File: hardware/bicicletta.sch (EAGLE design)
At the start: 27 parts, among them IC1 LM5017, IC2 LM1117-3.3

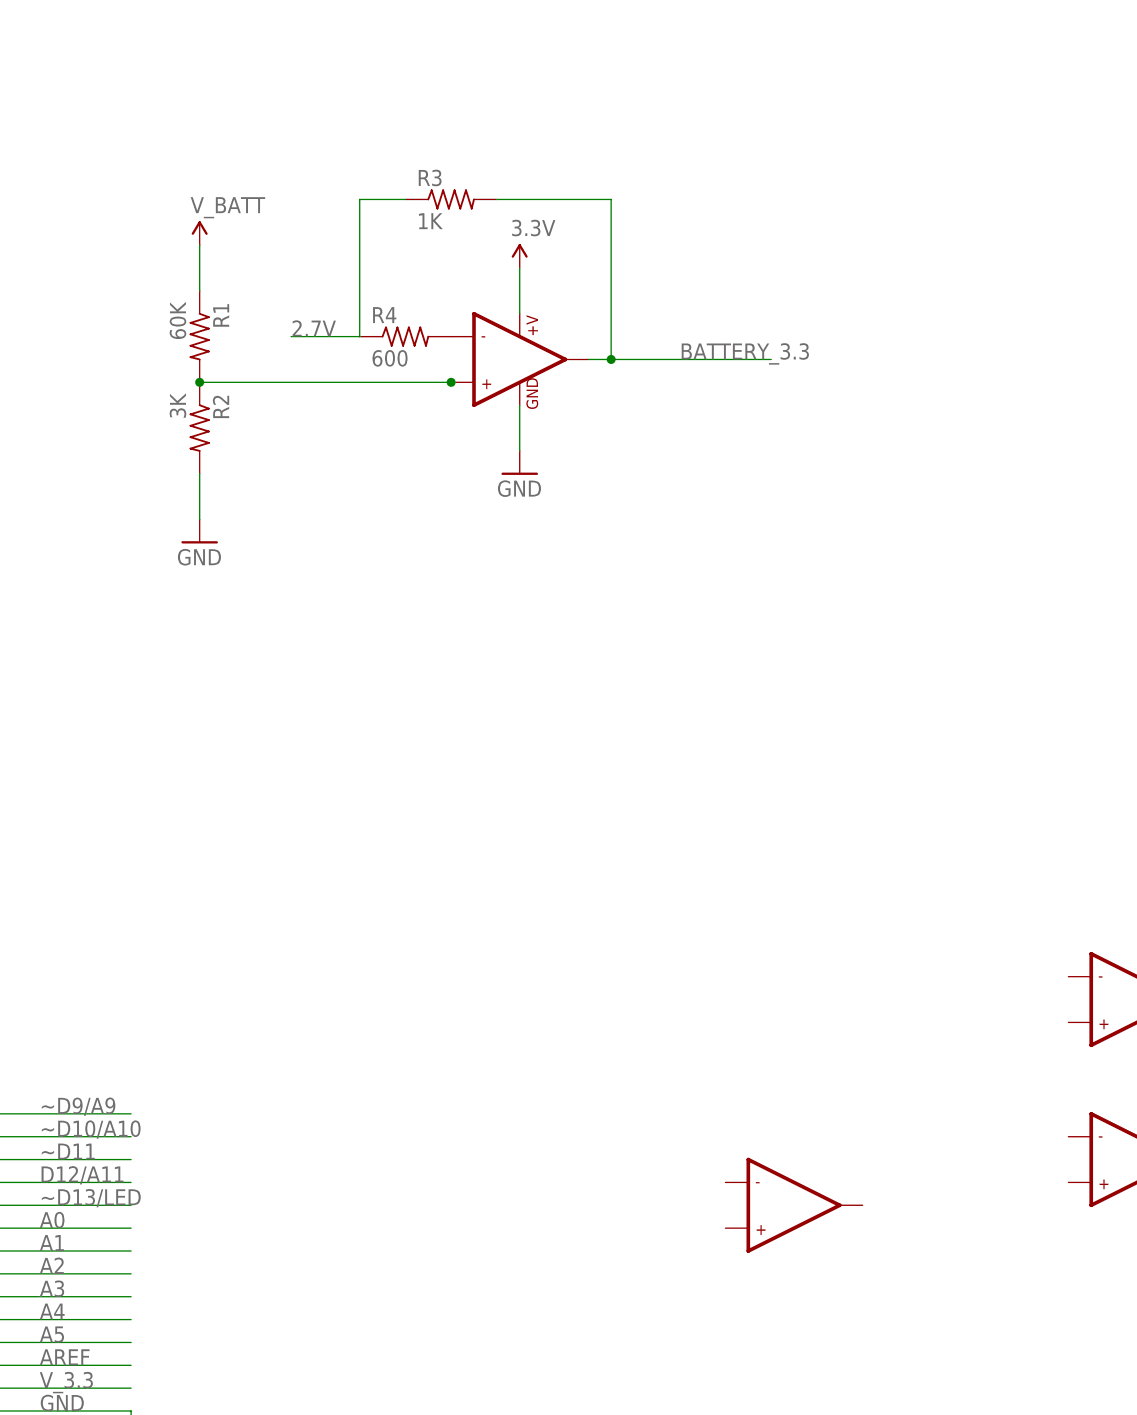
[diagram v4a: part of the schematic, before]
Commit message: Fixed battery voltage shifter, added level shifter for throttle (5V hall effect sensor)
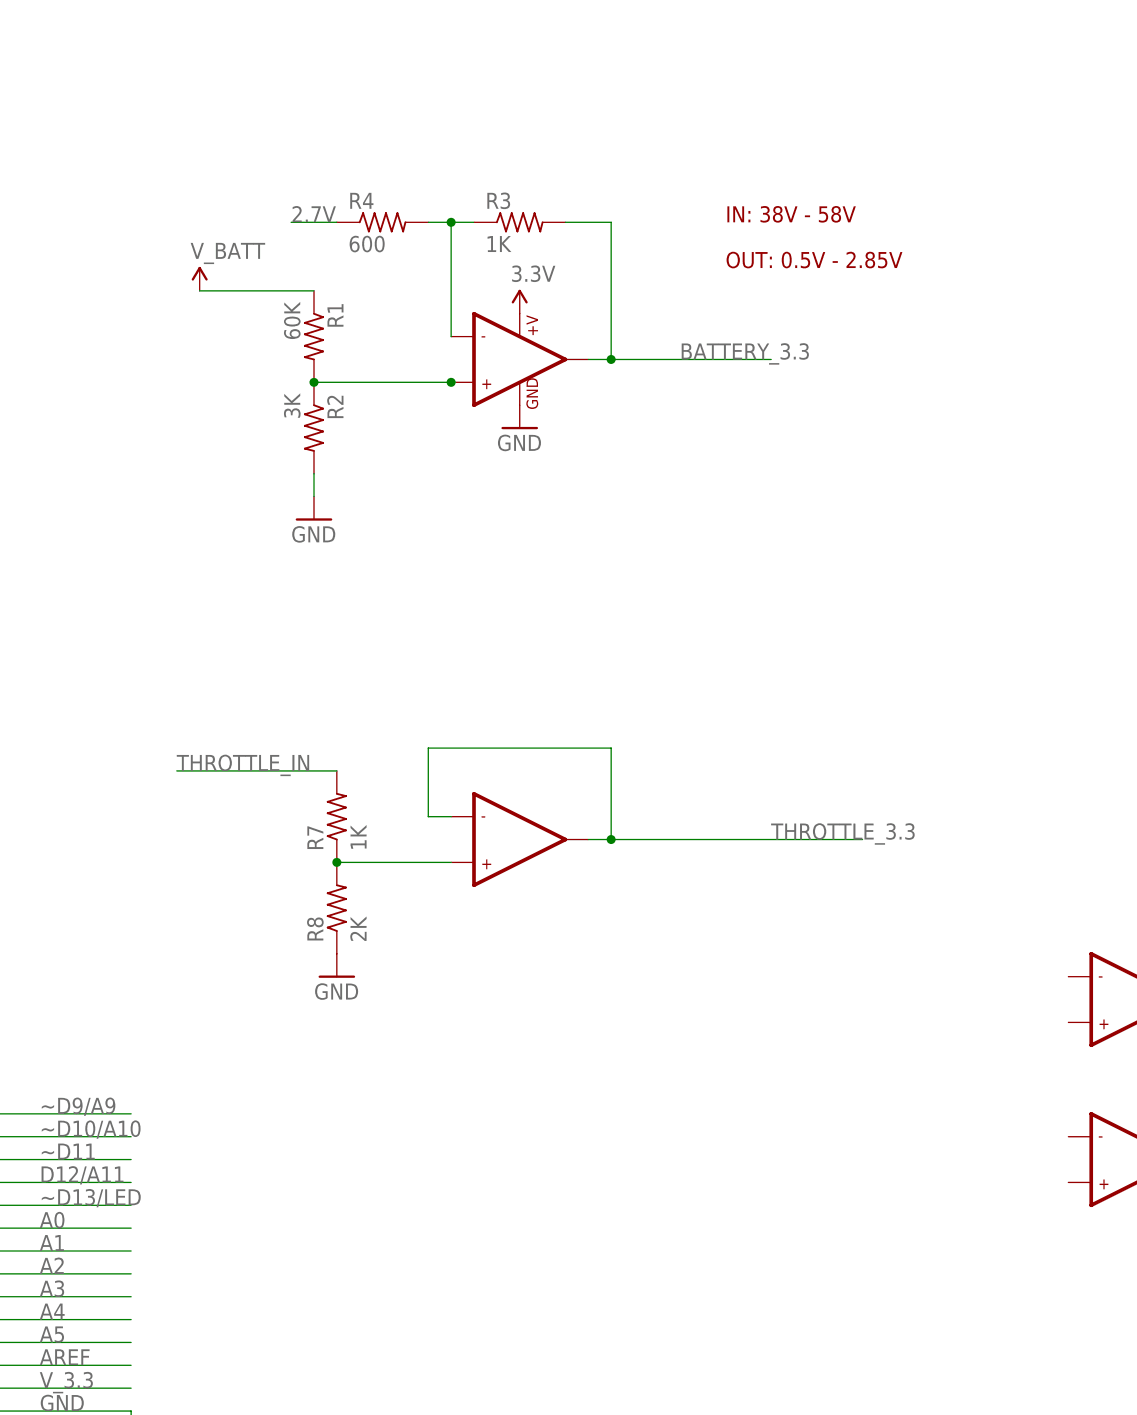
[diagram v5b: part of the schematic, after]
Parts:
- added R7: 1K, rcl:R-US_M0805
- added R8: 2K, rcl:R-US_M0805
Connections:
- new net N$11: R7.1, R8.2, U$1G$2.+IN2
- new net THROTTLE_3.3: U$1G$2.-IN2, U$1G$2.OUT2
- new net THROTTLE_IN: R7.2
- net 2.7V: no longer R3.1
- net GND: now also R8.1
- net N$10: now also R3.1
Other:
- note added: "IN: 38V - 58V"
- note added: "OUT: 0.5V - 2.85V"
- moved on the sheet: R1, R2, R3, R4
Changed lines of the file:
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@@
 <part name="GND7" library="SparkFun-Aesthetics" deviceset="GND" device=""/>
 <part name="U$4" library="SparkFun-Aesthetics" deviceset="V_BATT" device=""/>
+<part name="R7" library="rcl" deviceset="R-US_" device="M0805" value="1K"/>
+<part name="R8" library="rcl" deviceset="R-US_" device="M0805" value="2K"/>
+<part name="GND8" library="SparkFun-Aesthetics" deviceset="GND" device=""/>
 </parts>
 <sheets>
 <sheet>
 <plain>
+<text x="162.56" y="170.18" size="1.778" layer="94">IN: 38V - 58V</text>
+<text x="162.56" y="165.1" size="1.778" layer="94">OUT: 0.5V - 2.85V</text>
 </plain>
 <instances>
@@
 <instance part="JP2" gate="G$1" x="71.12" y="55.88"/>
 <instance part="U$1" gate="G$1" x="139.7" y="154.94"/>
-<instance part="U$1" gate="G$2" x="170.18" y="60.96"/>
+<instance part="U$1" gate="G$2" x="139.7" y="101.6"/>
 <instance part="U$2" gate="G$1" x="208.28" y="83.82"/>
 <instance part="U$2" gate="G$2" x="208.28" y="66.04"/>
@@
 <instance part="C1" gate="G$1" x="172.72" y="236.22"/>
 <instance part="C2" gate="G$1" x="208.28" y="236.22"/>
-<instance part="R1" gate="G$1" x="104.14" y="157.48" rot="R270"/>
-<instance part="R2" gate="G$1" x="104.14" y="147.32" rot="R270"/>
-<instance part="GND5" gate="1" x="104.14" y="134.62"/>
-<instance part="R3" gate="G$1" x="132.08" y="172.72"/>
-<instance part="R4" gate="G$1" x="127" y="157.48"/>
+<instance part="R1" gate="G$1" x="116.84" y="157.48" rot="R270"/>
+<instance part="R2" gate="G$1" x="116.84" y="147.32" rot="R270"/>
+<instance part="GND5" gate="1" x="116.84" y="137.16"/>
+<instance part="R3" gate="G$1" x="139.7" y="170.18"/>
+<instance part="R4" gate="G$1" x="124.46" y="170.18"/>
 <instance part="R5" gate="G$1" x="55.88" y="157.48" rot="R90"/>
 <instance part="R6" gate="G$1" x="55.88" y="147.32" rot="R90"/>
-<instance part="GND6" gate="1" x="139.7" y="142.24"/>
-<instance part="P+2" gate="G$1" x="139.7" y="165.1"/>
+<instance part="GND6" gate="1" x="139.7" y="147.32"/>
+<instance part="P+2" gate="G$1" x="139.7" y="160.02"/>
 <instance part="P+3" gate="G$1" x="55.88" y="165.1"/>
 <instance part="GND7" gate="1" x="55.88" y="137.16"/>
-<instance part="U$4" gate="G$1" x="104.14" y="167.64"/>
+<instance part="U$4" gate="G$1" x="104.14" y="162.56"/>
+<instance part="R7" gate="G$1" x="119.38" y="104.14" rot="R90"/>
+<instance part="R8" gate="G$1" x="119.38" y="93.98" rot="R90"/>
+<instance part="GND8" gate="1" x="119.38" y="86.36"/>
 </instances>
 <busses>
@@
 <pinref part="R2" gate="G$1" pin="2"/>
 <pinref part="GND5" gate="1" pin="GND"/>
-<wire x1="104.14" y1="137.16" x2="104.14" y2="142.24" width="0.1524" layer="91"/>
+<wire x1="116.84" y1="139.7" x2="116.84" y2="142.24" width="0.1524" layer="91"/>
 </segment>
 <segment>
 <pinref part="U$1" gate="G$1" pin="GND"/>
 <pinref part="GND6" gate="1" pin="GND"/>
-<wire x1="139.7" y1="144.78" x2="139.7" y2="149.86" width="0.1524" layer="91"/>
 </segment>
 <segment>
@@
 <wire x1="55.88" y1="139.7" x2="55.88" y2="142.24" width="0.1524" layer="91"/>
 <pinref part="GND7" gate="1" pin="GND"/>
+</segment>
+<segment>
+<pinref part="R8" gate="G$1" pin="1"/>
+<pinref part="GND8" gate="1" pin="GND"/>
 </segment>
 </net>
@@
 <segment>
 <pinref part="R1" gate="G$1" pin="1"/>
-<wire x1="104.14" y1="167.64" x2="104.14" y2="162.56" width="0.1524" layer="91"/>
+<wire x1="104.14" y1="162.56" x2="116.84" y2="162.56" width="0.1524" layer="91"/>
 <pinref part="U$4" gate="G$1" pin="1.8V"/>
 </segment>
@@
 <pinref part="U$1" gate="G$1" pin="+V"/>
 <pinref part="P+2" gate="G$1" pin="3.3V"/>
-<wire x1="139.7" y1="165.1" x2="139.7" y2="160.02" width="0.1524" layer="91"/>
 </segment>
 <segment>
@@
 <junction x="132.08" y="152.4"/>
 <pinref part="U$1" gate="G$1" pin="+IN1"/>
-<wire x1="132.08" y1="152.4" x2="104.14" y2="152.4" width="0.1524" layer="91"/>
-<junction x="104.14" y="152.4"/>
+<wire x1="132.08" y1="152.4" x2="116.84" y2="152.4" width="0.1524" layer="91"/>
+<junction x="116.84" y="152.4"/>
 </segment>
 </net>
@@
 <pinref part="R3" gate="G$1" pin="2"/>
 <wire x1="149.86" y1="154.94" x2="167.64" y2="154.94" width="0.1524" layer="91"/>
-<wire x1="137.16" y1="172.72" x2="149.86" y2="172.72" width="0.1524" layer="91"/>
-<wire x1="149.86" y1="172.72" x2="149.86" y2="154.94" width="0.1524" layer="91"/>
+<wire x1="144.78" y1="170.18" x2="149.86" y2="170.18" width="0.1524" layer="91"/>
+<wire x1="149.86" y1="170.18" x2="149.86" y2="154.94" width="0.1524" layer="91"/>
 <junction x="149.86" y="154.94"/>
 </segment>
@@
 <segment>
 <pinref part="R4" gate="G$1" pin="2"/>
+<pinref part="R3" gate="G$1" pin="1"/>
+<wire x1="129.54" y1="170.18" x2="132.08" y2="170.18" width="0.1524" layer="91"/>
 <pinref part="U$1" gate="G$1" pin="-IN1"/>
+<wire x1="132.08" y1="170.18" x2="134.62" y2="170.18" width="0.1524" layer="91"/>
+<wire x1="132.08" y1="157.48" x2="132.08" y2="170.18" width="0.1524" layer="91"/>
+<junction x="132.08" y="170.18"/>
 </segment>
 </net>
 <net name="2.7V" class="0">
-<segment>
-<pinref part="R3" gate="G$1" pin="1"/>
-<pinref part="R4" gate="G$1" pin="1"/>
-<wire x1="127" y1="172.72" x2="121.92" y2="172.72" width="0.1524" layer="91"/>
-<wire x1="121.92" y1="172.72" x2="121.92" y2="157.48" width="0.1524" layer="91"/>
-<label x="114.3" y="157.48" size="1.778" layer="95"/>
-<wire x1="121.92" y1="157.48" x2="114.3" y2="157.48" width="0.1524" layer="91"/>
-</segment>
 <segment>
 <pinref part="R6" gate="G$1" pin="2"/>
@@
 <label x="63.5" y="152.4" size="1.778" layer="95"/>
 </segment>
-</net>
+<segment>
+<pinref part="R4" gate="G$1" pin="1"/>
+<wire x1="119.38" y1="170.18" x2="114.3" y2="170.18" width="0.1524" layer="91"/>
+<label x="114.3" y="170.18" size="1.778" layer="95"/>
+</segment>
+</net>
+<net name="THROTTLE_IN" class="0">
+<segment>
+<label x="101.6" y="109.22" size="1.778" layer="95"/>
+<wire x1="119.38" y1="109.22" x2="101.6" y2="109.22" width="0.1524" layer="91"/>
+<pinref part="R7" gate="G$1" pin="2"/>
+</segment>
+</net>
+<net name="THROTTLE_3.3" class="0">
+<segment>
+<pinref part="U$1" gate="G$2" pin="OUT2"/>
+<label x="167.64" y="101.6" size="1.778" layer="95"/>
+<wire x1="147.32" y1="101.6" x2="149.86" y2="101.6" width="0.1524" layer="91"/>
+<pinref part="U$1" gate="G$2" pin="-IN2"/>
+<wire x1="149.86" y1="101.6" x2="177.8" y2="101.6" width="0.1524" layer="91"/>
+<wire x1="132.08" y1="104.14" x2="129.54" y2="104.14" width="0.1524" layer="91"/>
+<wire x1="129.54" y1="104.14" x2="129.54" y2="111.76" width="0.1524" layer="91"/>
+<wire x1="129.54" y1="111.76" x2="149.86" y2="111.76" width="0.1524" layer="91"/>
+<wire x1="149.86" y1="111.76" x2="149.86" y2="101.6" width="0.1524" layer="91"/>
+<junction x="149.86" y="101.6"/>
+</segment>
+</net>
+<net name="N$11" class="0">
+<segment>
+<pinref part="R7" gate="G$1" pin="1"/>
+<pinref part="R8" gate="G$1" pin="2"/>
+<pinref part="U$1" gate="G$2" pin="+IN2"/>
+<wire x1="132.08" y1="99.06" x2="119.38" y2="99.06" width="0.1524" layer="91"/>
+<junction x="119.38" y="99.06"/>
+</segment>
+</net>

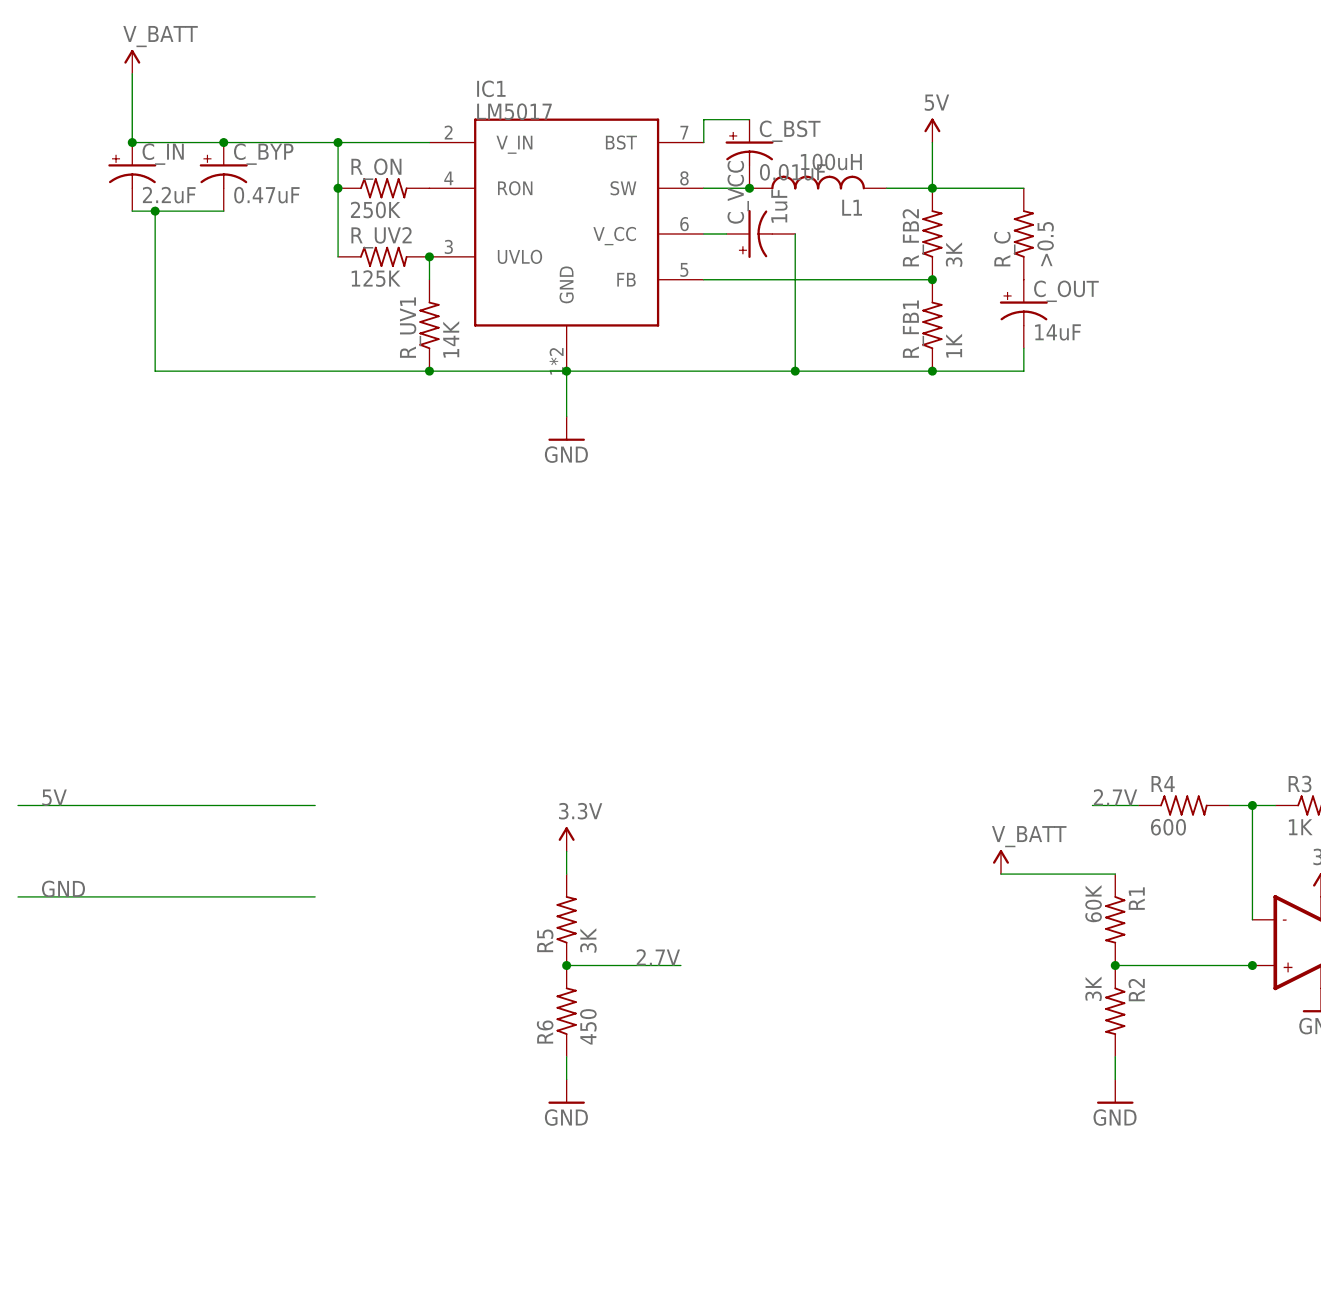
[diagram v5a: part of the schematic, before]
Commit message: Refactored the ripple feedback circuit on the switching regulator
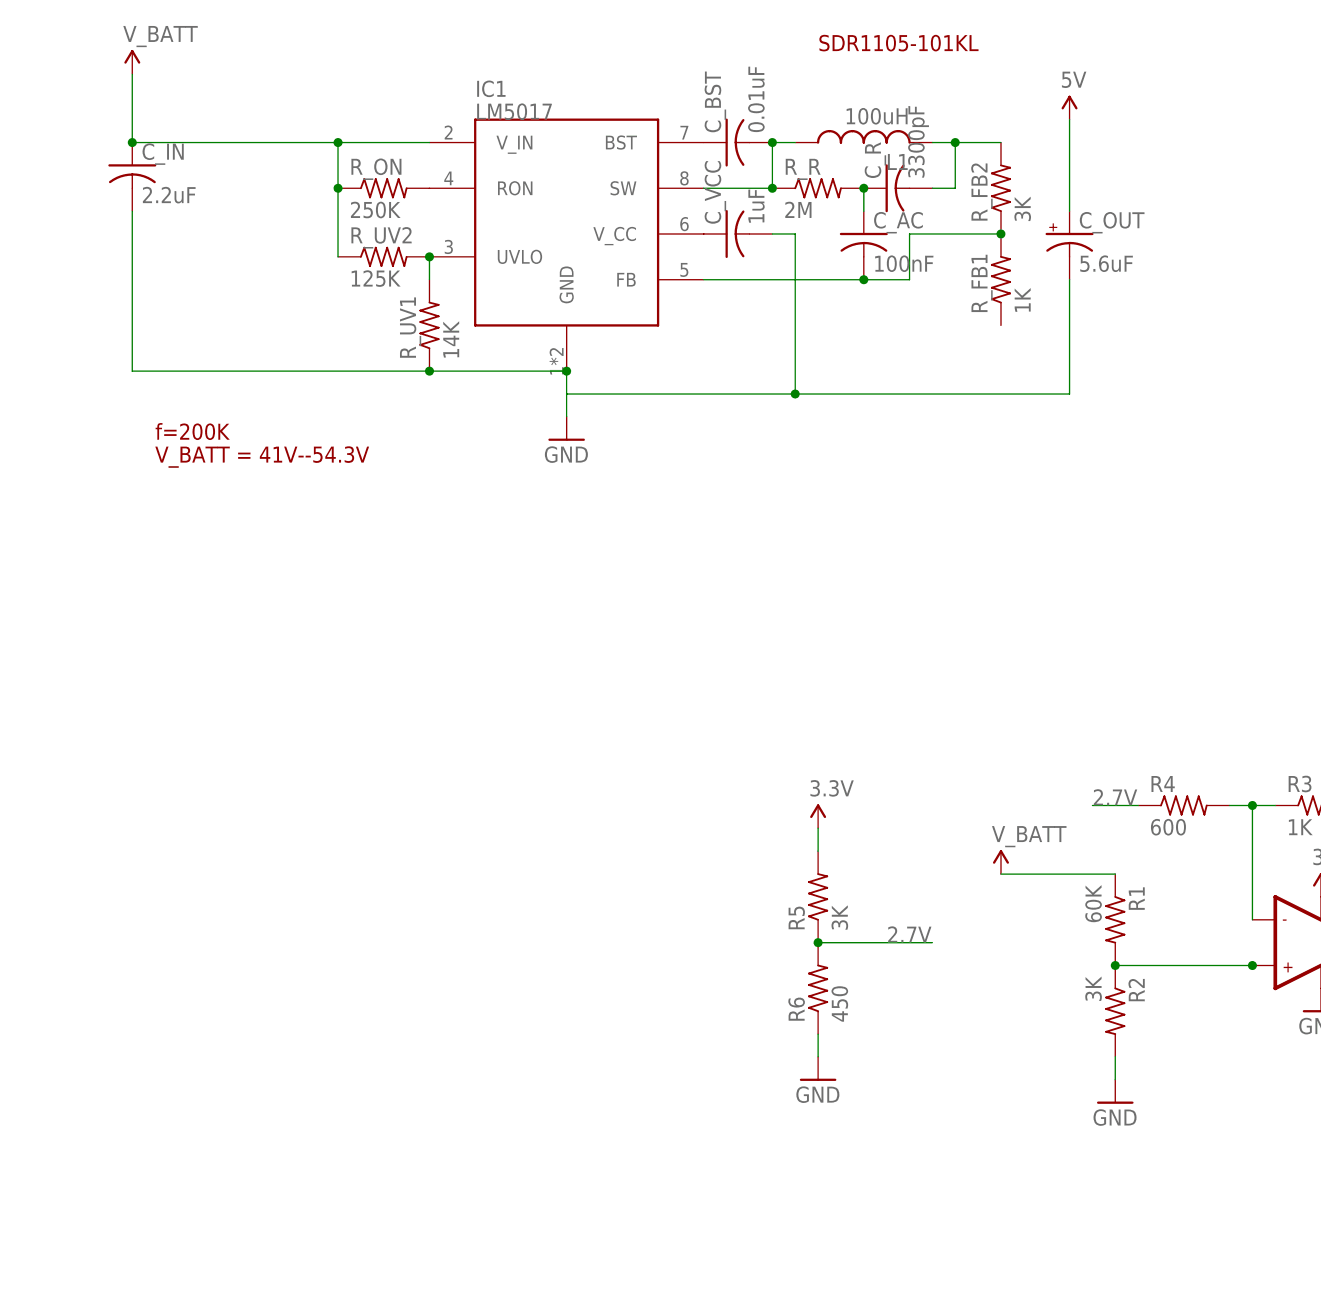
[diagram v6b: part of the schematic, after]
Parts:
- removed C_BYP: 0.47uF, rcl:CPOL-USUD-5X5,8
- removed R_C: >0.5, rcl:R-US_M0805
- added C_AC: 100nF, rcl:C-USC0603
- added C_R: 3300pF, rcl:C-USC0603
- added R_R: 2M, rcl:R-US_M0805
- C_BST, C_VCC: device rcl:CPOL-USUD-5X5,8 -> rcl:C-USC0603
- C_IN: device rcl:CPOL-USUD-5X5,8 -> rcl:C-USC1210K
- C_OUT: value 14uF -> 5.6uF
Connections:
- new net N$9: C_VCC.1, IC1.V_CC
- net 5V: now also C_OUT.+; no longer L1.2, R_C.2, R_FB2.2
- net GND: now also C_IN.2, C_VCC.2; no longer C_BYP.-, C_IN.-, C_VCC.-, R_FB1.1
- net N$2: now also C_AC.2
- net N$4: now also C_BST.2, IC1.SW, L1.1, R_R.1; no longer C_VCC.+, IC1.V_CC
- net N$5: now also C_R.2, L1.2, R_FB2.2; no longer C_BST.-, IC1.SW, L1.1
- net N$6: now also C_AC.1, C_R.1, R_R.2; no longer C_BST.+, IC1.BST
- net N$7: now also C_BST.1, IC1.BST; no longer C_OUT.+, R_C.1
- net V_BATT: now also C_IN.1; no longer C_BYP.+, C_IN.+
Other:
- note added: "SDR1105-101KL"
- note added: "V_BATT = 41V--54.3V"
- note added: "f=200K"
- moved on the sheet: C_OUT, L1, R5, R6, R_FB1, R_FB2
